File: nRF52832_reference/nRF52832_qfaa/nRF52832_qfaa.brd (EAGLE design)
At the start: 20 x 14 mm, 16 parts, among them U1 NRF52832, X1 32MHz, X2 32.768kHz

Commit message: Added more vias
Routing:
- net GND: vias 14 -> 23
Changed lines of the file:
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@@
 <vertex x="20" y="0"/>
 </polygon>
+<via x="0.9" y="13.1" extent="1-16" drill="0.4" diameter="0.8"/>
+<via x="4.8" y="13.1" extent="1-16" drill="0.4" diameter="0.8"/>
+<via x="19.1" y="13.1" extent="1-16" drill="0.4" diameter="0.8"/>
+<via x="16.7" y="3.7" extent="1-16" drill="0.4" diameter="0.8"/>
+<via x="19.1" y="0.9" extent="1-16" drill="0.4" diameter="0.8"/>
+<via x="16.7" y="0.9" extent="1-16" drill="0.4" diameter="0.8"/>
+<via x="6.4" y="1.9" extent="1-16" drill="0.4" diameter="0.8"/>
+<via x="0.9" y="0.9" extent="1-16" drill="0.4" diameter="0.8"/>
+<via x="0.9" y="2.9" extent="1-16" drill="0.4" diameter="0.8"/>
 </signal>
 <signal name="DEC1">

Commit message: Issue #2: Fixed value of C7 from 100nF to 100pF
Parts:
- C7: value 100nF -> 100pF
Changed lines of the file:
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@@
 <attribute name="VALUE" x="16.1" y="6.3" size="1.27" layer="27"/>
 </element>
-<element name="C7" library="Nordic_nRF" package="RESC0402_N" value="100nF" x="16.8" y="9.3" smashed="yes">
+<element name="C7" library="Nordic_nRF" package="RESC0402_N" value="100pF" x="16.8" y="9.3" smashed="yes">
 <attribute name="NAME" x="16.3" y="9" size="0.6" layer="25"/>
 <attribute name="VALUE" x="16.1" y="7.3" size="1.27" layer="27"/>

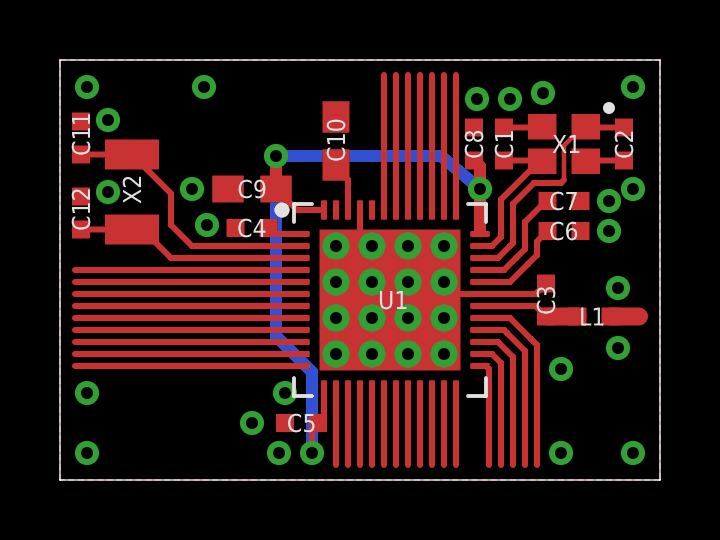
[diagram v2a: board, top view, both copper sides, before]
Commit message: Same fixes as in qfaa_dcdc
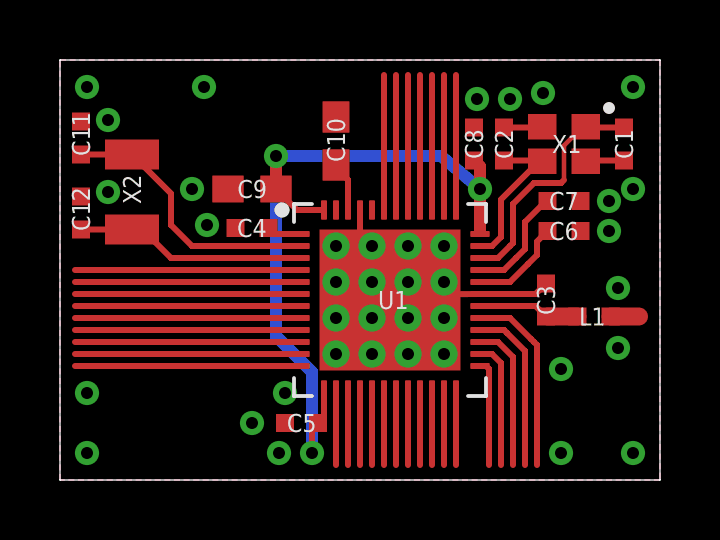
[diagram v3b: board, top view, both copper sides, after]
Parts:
- moved C1 4.00 mm to (18.8, 11.2), turned to 270 degrees
- moved C2 4.00 mm to (14.8, 11.2), turned to 90 degrees
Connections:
- removed net P0.01: U1.11
- new net P0.10: U1.12
- net N$3: now also C2.1; no longer C1.1
- net P0.09: now also U1.11; no longer U1.12
- net X1: now also C1.1; no longer C2.1
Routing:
- net P0.10: track 0.00 -> 7.50 mm
- net P0.01: track 7.50 -> 0.00 mm
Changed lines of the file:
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@@
 <?xml version="1.0" encoding="utf-8"?>
 <!DOCTYPE eagle SYSTEM "eagle.dtd">
-<eagle version="7.6.0">
+<eagle version="8.3.0">
 <drawing>
 <settings>
 <setting alwaysvectorfont="no"/>
+<setting keepoldvectorfont="yes"/>
 <setting verticaltext="up"/>
 </settings>
@@
 <attribute name="VALUE" x="17.1" y="3.45" size="1.27" layer="27"/>
 </element>
-<element name="C1" library="Nordic_nRF" package="RESC0402_N" value="12pF" x="14.8" y="11.2" smashed="yes" rot="R90">
+<element name="C2" library="Nordic_nRF" package="RESC0402_N" value="12pF" x="14.8" y="11.2" smashed="yes" rot="R90">
 <attribute name="NAME" x="15.1" y="10.7" size="0.6" layer="25" rot="R90"/>
 <attribute name="VALUE" x="16.8" y="10.5" size="1.27" layer="27" rot="R90"/>
 </element>
-<element name="C2" library="Nordic_nRF" package="RESC0402_N" value="12pF" x="18.8" y="11.2" smashed="yes" rot="R270">
+<element name="C1" library="Nordic_nRF" package="RESC0402_N" value="12pF" x="18.8" y="11.2" smashed="yes" rot="R270">
 <attribute name="NAME" x="19.1" y="10.7" size="0.6" layer="25" rot="R90"/>
 <attribute name="VALUE" x="16.8" y="11.9" size="1.27" layer="27" rot="R270"/>
@@
 <contactref element="X1" pad="4"/>
 <contactref element="X1" pad="2"/>
+<contactref element="C2" pad="2"/>
 <contactref element="C1" pad="2"/>
-<contactref element="C2" pad="2"/>
 <contactref element="C3" pad="2"/>
 <contactref element="C4" pad="2"/>
@@
 <contactref element="U1" pad="35"/>
 <contactref element="X1" pad="3"/>
-<contactref element="C1" pad="1"/>
+<contactref element="C2" pad="1"/>
 <wire x1="14" y1="7.8" x2="14.4" y2="7.8" width="0.2" layer="1"/>
 <wire x1="14.4" y1="7.8" x2="14.7" y2="8.1" width="0.2" layer="1"/>
@@
 <contactref element="U1" pad="34"/>
 <contactref element="X1" pad="1"/>
-<contactref element="C2" pad="1"/>
+<contactref element="C1" pad="1"/>
 <wire x1="18.8" y1="11.75" x2="17.55" y2="11.75" width="0.2" layer="1"/>
 <wire x1="17.55" y1="11.75" x2="17.525" y2="11.775" width="0.2" layer="1"/>
@@
 <wire x1="18.35" y1="5.45" x2="19.3" y2="5.45" width="0.6" layer="1"/>
 </signal>
-<signal name="P0.09">
+<signal name="P0.10">
 <contactref element="U1" pad="12"/>
 <wire x1="8" y1="3.8" x2="0.5" y2="3.8" width="0.2" layer="1"/>
 </signal>
-<signal name="P0.01">
+<signal name="P0.09">
 <contactref element="U1" pad="11"/>
 <wire x1="8" y1="4.2" x2="0.5" y2="4.2" width="0.2" layer="1"/>
